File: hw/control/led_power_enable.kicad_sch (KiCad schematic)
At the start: 7 parts, among them Q1201 BC807, Q1202 BC817

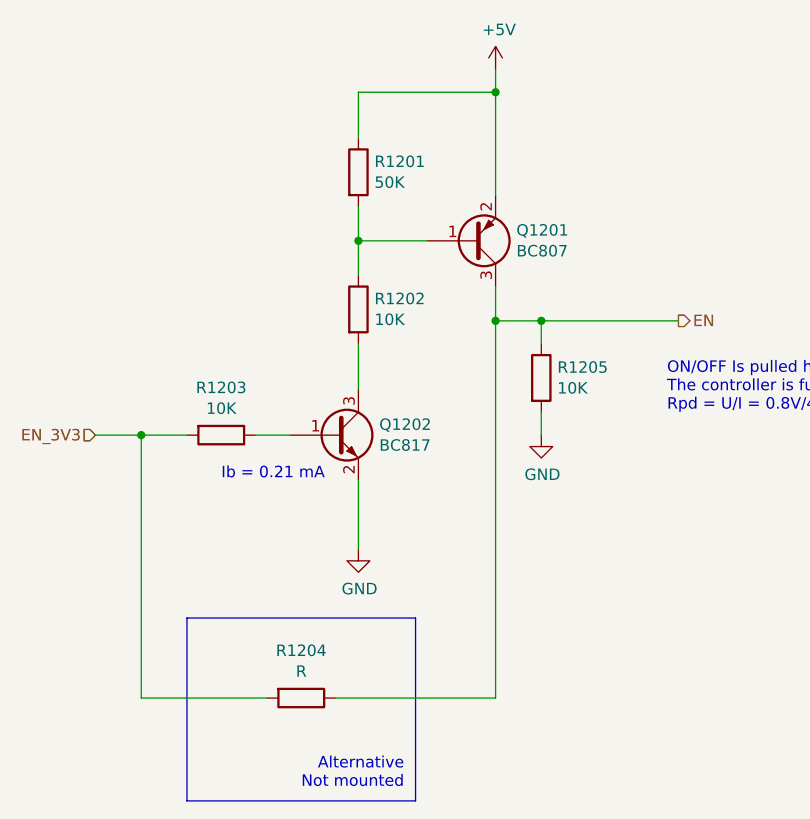
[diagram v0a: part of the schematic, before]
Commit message: [hw] Update to KiCAD 7
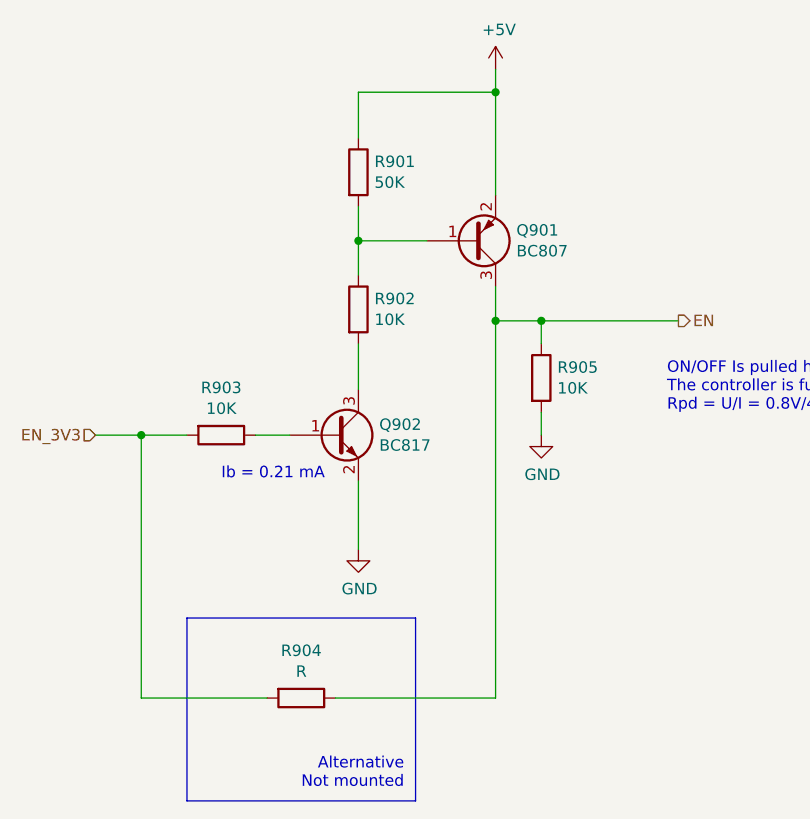
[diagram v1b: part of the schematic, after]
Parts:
- renumbered Q1201 to Q901, Q1202 to Q902, R1201 to R901, R1202 to R902, R1203 to R903, R1204 to R904, R1205 to R905
